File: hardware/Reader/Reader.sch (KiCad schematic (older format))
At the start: 13 parts, among them U1 MAX25276ATCA_VY+, U2 STN2120, X1 16MHz

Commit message: Revised initial schematics for hierarhical structure. Added ESP32, 'Power Supply', Reader MEMs and Power Switch. OBD-II Interpreter is work-in-progress
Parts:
- removed C1, C2: 1uF, symbol Device:C
- removed Cbst1: 0.1uF, symbol Device:C
- removed Cin1: 4.7 uF, symbol Device:CP
- removed Cl1: 0.1 uF, symbol Device:CP
- removed Cout1: 22uF, symbol Device:C
- removed JP1: Reset NVM???, symbol Device:Jumper
- removed L1: 4.7 uH, symbol Device:L
- removed R10, R7: 100k, symbol Device:R
- removed U1: MAX25276ATCA_VY+, 21-100284A_TD1233Y+3C_MXM, symbol MAX25276ATCAVY:MAX25276ATCA_VY+
- removed U2: STN2120, symbol CANtech:STN2120
- removed X1: 16MHz, symbol Device:Crystal_GND24
- added ESP32: NodeMCU_ESP32_DevKit, symbol CANtech:NodeMCU_ESP32_DevKit
- added Rdown: R???, symbol Device:R_Small
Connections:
- net labels added: +5V, GND, Pin10_SAE_J1850_BUS-, Pin11_MS_CAN_Low, Pin12, Pin13, Pin14_ISO15765-4_CAN_BUS_Low, Pin15_ISO9141_L-Line, Pin16_Raw_+12V_Battery, Pin1_SW_CAN, Pin2_SAE_J1850_BUS+, Pin3_MS_CAN_High, Pin4_GnD_Chassis, Pin5_Gnd_Signal, Pin6_ISO15765-4_CAN_BUS_High, Pin7_ISO9141_K-Line, Pin8, Pin9
- net labels removed: +12V, ESP32, GNDPWR, GNDREF
- wire segments 74 -> 38
- no-connect marks 0 -> 4
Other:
- note added: "OBD-II Connector/Data Link Connector"

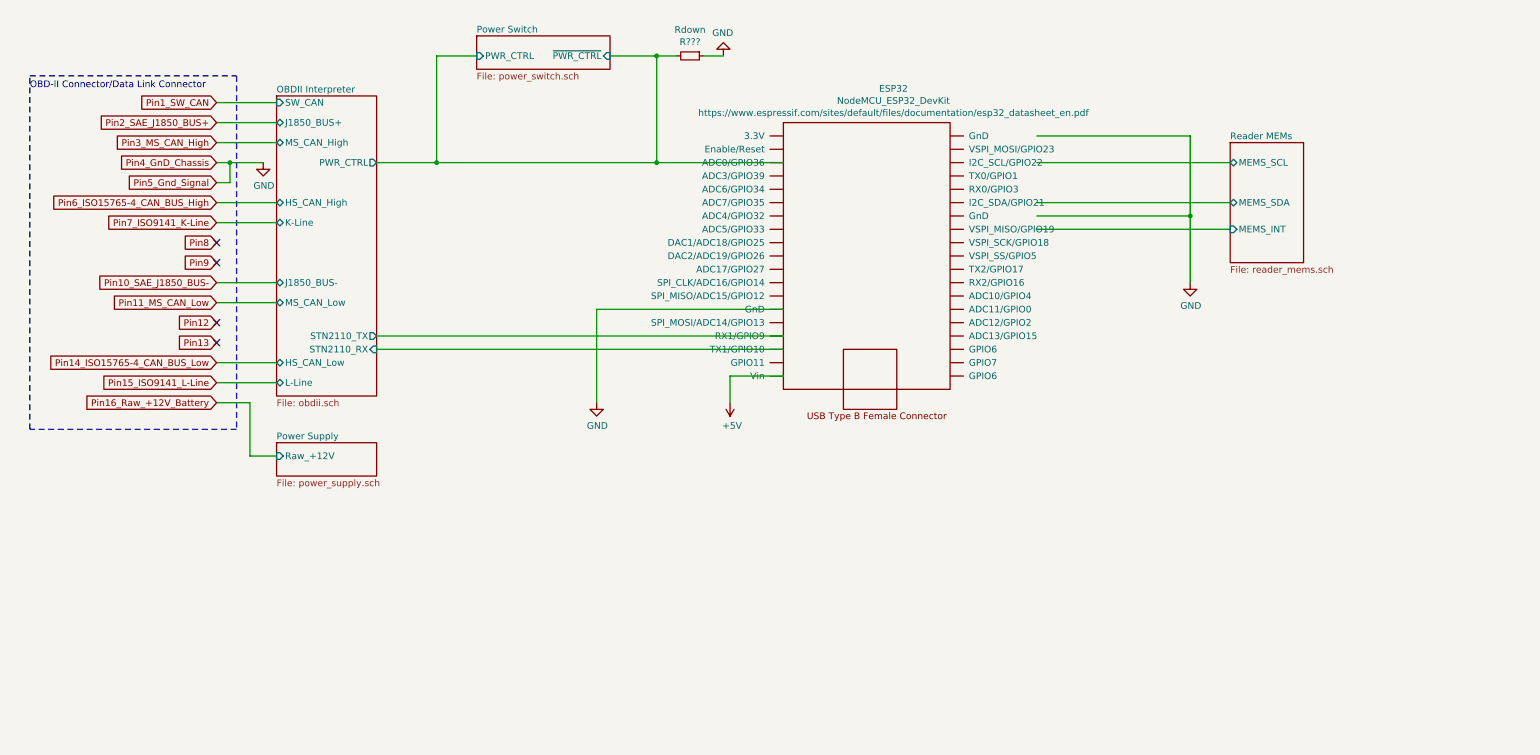
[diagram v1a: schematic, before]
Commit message: Completed schematics for reader
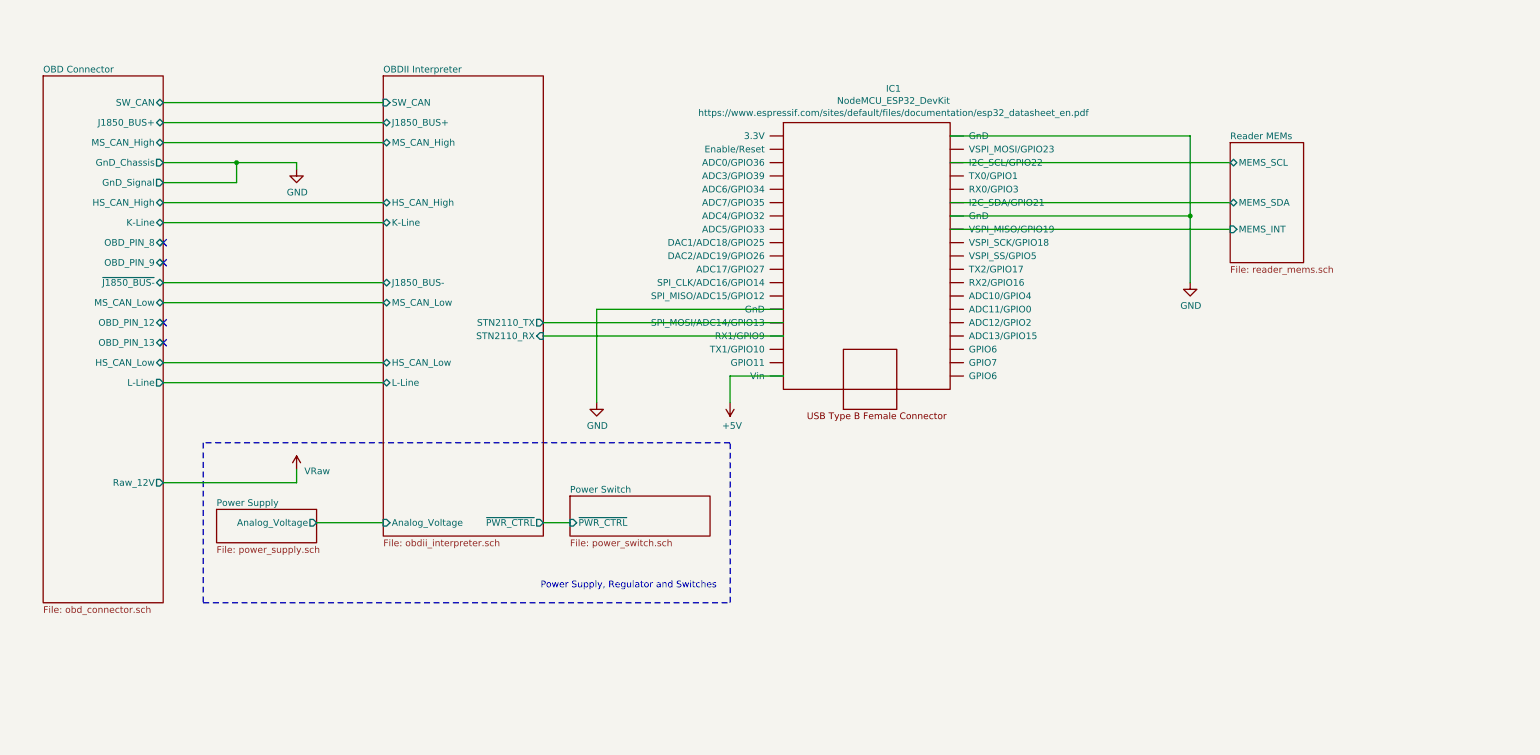
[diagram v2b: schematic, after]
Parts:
- removed Rdown: R???, symbol Device:R_Small
- renumbered ESP32 to IC1
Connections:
- net labels added: VRaw
- net labels removed: Pin10_SAE_J1850_BUS-, Pin11_MS_CAN_Low, Pin12, Pin13, Pin14_ISO15765-4_CAN_BUS_Low, Pin15_ISO9141_L-Line, Pin16_Raw_+12V_Battery, Pin1_SW_CAN, Pin2_SAE_J1850_BUS+, Pin3_MS_CAN_High, Pin4_GnD_Chassis, Pin5_Gnd_Signal, Pin6_ISO15765-4_CAN_BUS_High, Pin7_ISO9141_K-Line, Pin8, Pin9
- wire segments 38 -> 31
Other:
- note added: "Power Supply, Regulator and Switches"
- note removed: "OBD-II Connector/Data Link Connector"
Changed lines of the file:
@@
 $Descr USLetter 11000 8500
 encoding utf-8
-Sheet 1 9
+Sheet 1 17
 Title "CANnect Reader"
-Date "2020-10-18"
+Date "2020-10-20"
 Rev "0.0.1"
 Comp "CANtech"
-Comment1 ""
+Comment1 "Created by Choong Jin Ng | jin8383@gmail.com"
 Comment2 ""
 Comment3 ""
 Comment4 ""
 $EndDescr
-Text GLabel 2000 3650 0    50   Input ~ 0
-Pin16_Raw_+12V_Battery
-Text GLabel 2000 1850 0    50   Input ~ 0
-Pin4_GnD_Chassis
-Text GLabel 2000 2000 0    50   Input ~ 0
-Pin5_Gnd_Signal
-Text GLabel 2000 2450 0    50   Input ~ 0
-Pin8
-Text GLabel 2000 2600 0    50   Input ~ 0
-Pin9
-Text GLabel 2000 3050 0    50   Input ~ 0
-Pin12
-Text GLabel 2000 3200 0    50   Input ~ 0
-Pin13
-NoConn ~ 2000 3050
-NoConn ~ 2000 3200
-NoConn ~ 2000 2600
-NoConn ~ 2000 2450
-Wire Wire Line
-	2000 1850 2100 1850
-Wire Wire Line
-	2000 2000 2100 2000
-Wire Wire Line
-	2100 2000 2100 1850
-Connection ~ 2100 1850
-Wire Wire Line
-	2100 1850 2350 1850
-$Comp
-L power:GND #PWR0101
-U 1 1 5F8F20F1
-P 2350 1850
-F 0 "#PWR0101" H 2350 1600 50  0001 C CNN
-F 1 "GND" H 2355 1677 50  0000 C CNN
-F 2 "" H 2350 1850 50  0001 C CNN
-F 3 "" H 2350 1850 50  0001 C CNN
-	1    2350 1850
-	1    0    0    -1
-$EndComp
 $Comp
 L power:GND #PWR0102
@@
 $EndComp
 $Sheet
-S 2450 3950 750  250
+S 2000 4450 750  250
 U 5F8ADA45
 F0 "Power Supply" 50
 F1 "power_supply.sch" 50
-F2 "Raw_+12V" I L 2450 4050 50
+F2 "Analog_Voltage" O R 2750 4550 50
 $EndSheet
 Wire Wire Line
@@
 Wire Wire Line
 	9300 2250 9300 2750
-Text GLabel 2000 2900 0    50   Input ~ 0
-Pin11_MS_CAN_Low
-Text GLabel 2000 1700 0    50   Input ~ 0
-Pin3_MS_CAN_High
-Text GLabel 2000 2750 0    50   Input ~ 0
-Pin10_SAE_J1850_BUS-
-Text GLabel 2000 1550 0    50   Input ~ 0
-Pin2_SAE_J1850_BUS+
-Text GLabel 2000 3350 0    50   Input ~ 0
-Pin14_ISO15765-4_CAN_BUS_Low
-Text GLabel 2000 2150 0    50   Input ~ 0
-Pin6_ISO15765-4_CAN_BUS_High
-Text GLabel 2000 3500 0    50   Input ~ 0
-Pin15_ISO9141_L-Line
-Text GLabel 2000 2300 0    50   Input ~ 0
-Pin7_ISO9141_K-Line
-Wire Wire Line
-	2000 2900 2450 2900
-Wire Wire Line
-	2000 1700 2450 1700
-Wire Wire Line
-	2000 2750 2450 2750
-Wire Wire Line
-	2000 1550 2450 1550
-Wire Wire Line
-	2000 3350 2450 3350
-Wire Wire Line
-	2000 2150 2450 2150
-Wire Wire Line
-	2000 3500 2450 3500
-Wire Wire Line
-	2000 2300 2450 2300
-Text GLabel 2000 1400 0    50   Input ~ 0
-Pin1_SW_CAN
-Wire Wire Line
-	2000 1400 2450 1400
-$Sheet
-S 2450 1350 750  2250
-U 5F95F80B
-F0 "OBDII Interpreter" 50
-F1 "obdii.sch" 50
-F2 "K-Line" B L 2450 2300 50
-F3 "L-Line" B L 2450 3500 50
-F4 "SW_CAN" I L 2450 1400 50
-F5 "J1850_BUS+" B L 2450 1550 50
-F6 "J1850_BUS-" B L 2450 2750 50
-F7 "MS_CAN_High" B L 2450 1700 50
-F8 "MS_CAN_Low" B L 2450 2900 50
-F9 "STN2110_TX" O R 3200 3150 50
-F10 "PWR_CTRL" O R 3200 1850 50
-F11 "HS_CAN_High" B L 2450 2150 50
-F12 "HS_CAN_Low" B L 2450 3350 50
-F13 "STN2110_RX" I R 3200 3250 50
-$EndSheet
-$Sheet
-S 3950 900  1000 250
+$Sheet
+S 4650 4350 1050 300
 U 5FA56A4E
 F0 "Power Switch" 50
 F1 "power_switch.sch" 50
-F2 "~PWR_CTRL~" I R 4950 1050 50
-F3 "PWR_CTRL" I L 3950 1050 50
+F2 "~PWR_CTRL~" I L 4650 4550 50
 $EndSheet
 $Sheet
@@
 F4 "MEMS_INT" I L 9600 2350 50
 $EndSheet
-Wire Wire Line
-	8150 2350 9600 2350
-Wire Wire Line
-	8150 2150 9600 2150
-Wire Wire Line
-	8150 1650 9300 1650
-Wire Wire Line
-	8150 2250 9300 2250
-Wire Wire Line
-	8150 1850 9600 1850
 $Comp
 L power:GND #PWR0104
@@
 	1    0    0    1
 $EndComp
-$Comp
-L CANtech:NodeMCU_ESP32_DevKit ESP32
+Wire Wire Line
+	5850 3650 5850 3450
+Wire Wire Line
+	5850 3450 6250 3450
+Wire Wire Line
+	4850 3650 4850 2950
+Wire Wire Line
+	4850 2950 6250 2950
+$Comp
+L CANtech:VRaw #V0101
+U 1 1 5FD58425
+P 2600 4100
+F 0 "#V0101" H 2600 4100 50  0001 C CNN
+F 1 "VRaw" H 2658 4037 50  0000 L CNN
+F 2 "" H 2600 4100 50  0001 C CNN
+F 3 "" H 2600 4100 50  0001 C CNN
+	1    2600 4100
+	1    0    0    -1
+$EndComp
+$Comp
+L CANtech:NodeMCU_ESP32_DevKit IC1
 U 1 1 5F91A3F3
 P 6900 4900
-F 0 "ESP32" H 7075 8505 50  0000 C CNN
+F 0 "IC1" H 7075 8505 50  0000 C CNN
 F 1 "NodeMCU_ESP32_DevKit" H 7075 8414 50  0000 C CNN
 F 2 "" H 6900 4900 50  0001 C CNN
@@
 $EndComp
 Wire Wire Line
-	5850 3650 5850 3450
-Wire Wire Line
-	5850 3450 6250 3450
-Wire Wire Line
-	4850 3650 4850 2950
-Wire Wire Line
-	4850 2950 6250 2950
-$Comp
-L power:GND #PWR?
-U 1 1 5FA7F77A
-P 5800 1050
-F 0 "#PWR?" H 5800 800 50  0001 C CNN
-F 1 "GND" H 5805 877 50  0000 C CNN
-F 2 "" H 5800 1050 50  0001 C CNN
-F 3 "" H 5800 1050 50  0001 C CNN
-	1    5800 1050
-	-1   0    0    1
-$EndComp
-Wire Wire Line
-	6250 1850 5300 1850
-Wire Wire Line
-	5300 1850 5300 1050
-Wire Wire Line
-	4950 1050 5300 1050
-$Comp
-L Device:R_Small Rdown
-U 1 1 5FA811AB
-P 5550 1050
-F 0 "Rdown" V 5354 1050 50  0000 C CNN
-F 1 "R???" V 5445 1050 50  0000 C CNN
-F 2 "" H 5550 1050 50  0001 C CNN
-F 3 "~" H 5550 1050 50  0001 C CNN
-	1    5550 1050
-	0    1    1    0
-$EndComp
-Wire Wire Line
-	5300 1050 5450 1050
-Connection ~ 5300 1050
-Wire Wire Line
-	5650 1050 5800 1050
-Wire Wire Line
-	5300 1850 3650 1850
-Connection ~ 5300 1850
-Wire Wire Line
-	3950 1050 3650 1050
-Wire Wire Line
-	3650 1050 3650 1850
-Connection ~ 3650 1850
-Wire Wire Line
-	3650 1850 3200 1850
-Wire Wire Line
-	3200 3150 6250 3150
-Wire Wire Line
-	6250 3250 3200 3250
-Wire Wire Line
-	2000 3650 2250 3650
-Wire Wire Line
-	2250 3650 2250 4050
-Wire Wire Line
-	2250 4050 2450 4050
-Wire Notes Line
-	2150 1200 2150 3850
-Wire Notes Line
-	2150 3850 600  3850
-Wire Notes Line
-	600  3850 600  1200
-Wire Notes Line
-	600  1200 2150 1200
-Text Notes 600  1300 0    50   ~ 0
-OBD-II Connector/Data Link Connector
+	2600 4250 2600 4150
+Wire Wire Line
+	2750 4550 3250 4550
+$Sheet
+S 3250 1200 1200 3450
+U 5F95F80B
+F0 "OBDII Interpreter" 50
+F1 "obdii_interpreter.sch" 50
+F2 "K-Line" B L 3250 2300 50
+F3 "L-Line" B L 3250 3500 50
+F4 "SW_CAN" I L 3250 1400 50
+F5 "J1850_BUS+" B L 3250 1550 50
+F6 "J1850_BUS-" B L 3250 2750 50
+F7 "MS_CAN_High" B L 3250 1700 50
+F8 "MS_CAN_Low" B L 3250 2900 50
+F9 "STN2110_TX" O R 4450 3050 50
+F10 "HS_CAN_High" B L 3250 2150 50
+F11 "HS_CAN_Low" B L 3250 3350 50
+F12 "STN2110_RX" I R 4450 3150 50
+F13 "~PWR_CTRL~" O R 4450 4550 50
+F14 "Analog_Voltage" I L 3250 4550 50
+$EndSheet
+Wire Wire Line
+	4450 4550 4650 4550
+Wire Notes Line
+	1900 3950 1900 5150
+Wire Notes Line
+	1900 5150 5850 5150
+Wire Notes Line
+	5850 5150 5850 3950
+Wire Notes Line
+	5850 3950 1900 3950
+Text Notes 5750 5050 2    50   ~ 0
+Power Supply, Regulator and Switches
+Wire Wire Line
+	4450 3050 6250 3050
+Wire Wire Line
+	6250 3150 4450 3150
+$Sheet
+S 700  1200 900  3950
+U 5FF6FE24
+F0 "OBD Connector" 50
+F1 "obd_connector.sch" 50
+F2 "SW_CAN" B R 1600 1400 50
+F3 "Raw_12V" O R 1600 4250 50
+F4 "J1850_BUS+" B R 1600 1550 50
+F5 "MS_CAN_High" B R 1600 1700 50
+F6 "GnD_Chassis" O R 1600 1850 50
+F7 "GnD_Signal" O R 1600 2000 50
+F8 "HS_CAN_High" B R 1600 2150 50
+F9 "K-Line" B R 1600 2300 50
+F10 "OBD_PIN_8" B R 1600 2450 50
+F11 "OBD_PIN_9" B R 1600 2600 50
+F12 "~J1850_BUS-~" B R 1600 2750 50
+F13 "MS_CAN_Low" B R 1600 2900 50
+F14 "OBD_PIN_12" B R 1600 3050 50
+F15 "OBD_PIN_13" B R 1600 3200 50
+F16 "HS_CAN_Low" B R 1600 3350 50
+F17 "L-Line" O R 1600 3500 50
+$EndSheet
+Wire Wire Line
+	1600 4250 2600 4250
+Wire Wire Line
+	1600 1400 3250 1400
+Wire Wire Line
+	1600 1550 3250 1550
+Wire Wire Line
+	3250 1700 1600 1700
+$Comp
+L power:GND #PWR01
+U 1 1 5FF8C892
+P 2600 1900
+F 0 "#PWR01" H 2600 1650 50  0001 C CNN
+F 1 "GND" H 2605 1727 50  0000 C CNN
+F 2 "" H 2600 1900 50  0001 C CNN
+F 3 "" H 2600 1900 50  0001 C CNN
+	1    2600 1900
+	1    0    0    -1
+$EndComp
+Wire Wire Line
+	1600 1850 2150 1850
+Wire Wire Line
+	2600 1850 2600 1900
+Wire Wire Line
+	1600 2000 2150 2000
+Wire Wire Line
+	2150 2000 2150 1850
+Connection ~ 2150 1850
+Wire Wire Line
+	2150 1850 2600 1850
+Wire Wire Line
+	1600 2150 3250 2150
+Wire Wire Line
+	1600 2300 3250 2300
+Wire Wire Line
+	1600 2750 3250 2750
+Wire Wire Line
+	3250 2900 1600 2900
+Wire Wire Line
+	1600 3350 3250 3350
+Wire Wire Line
+	3250 3500 1600 3500
+NoConn ~ 1600 2450
+NoConn ~ 1600 2600
+NoConn ~ 1600 3050
+NoConn ~ 1600 3200
+Wire Wire Line
+	7500 1650 9300 1650
+Wire Wire Line
+	7500 2150 9600 2150
+Wire Wire Line
+	7500 2250 9300 2250
+Wire Wire Line
+	7500 2350 9600 2350
+Wire Wire Line
+	7500 1850 9600 1850
 $EndSCHEMATC

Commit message: Completed Reader schematics for version 0.0.01
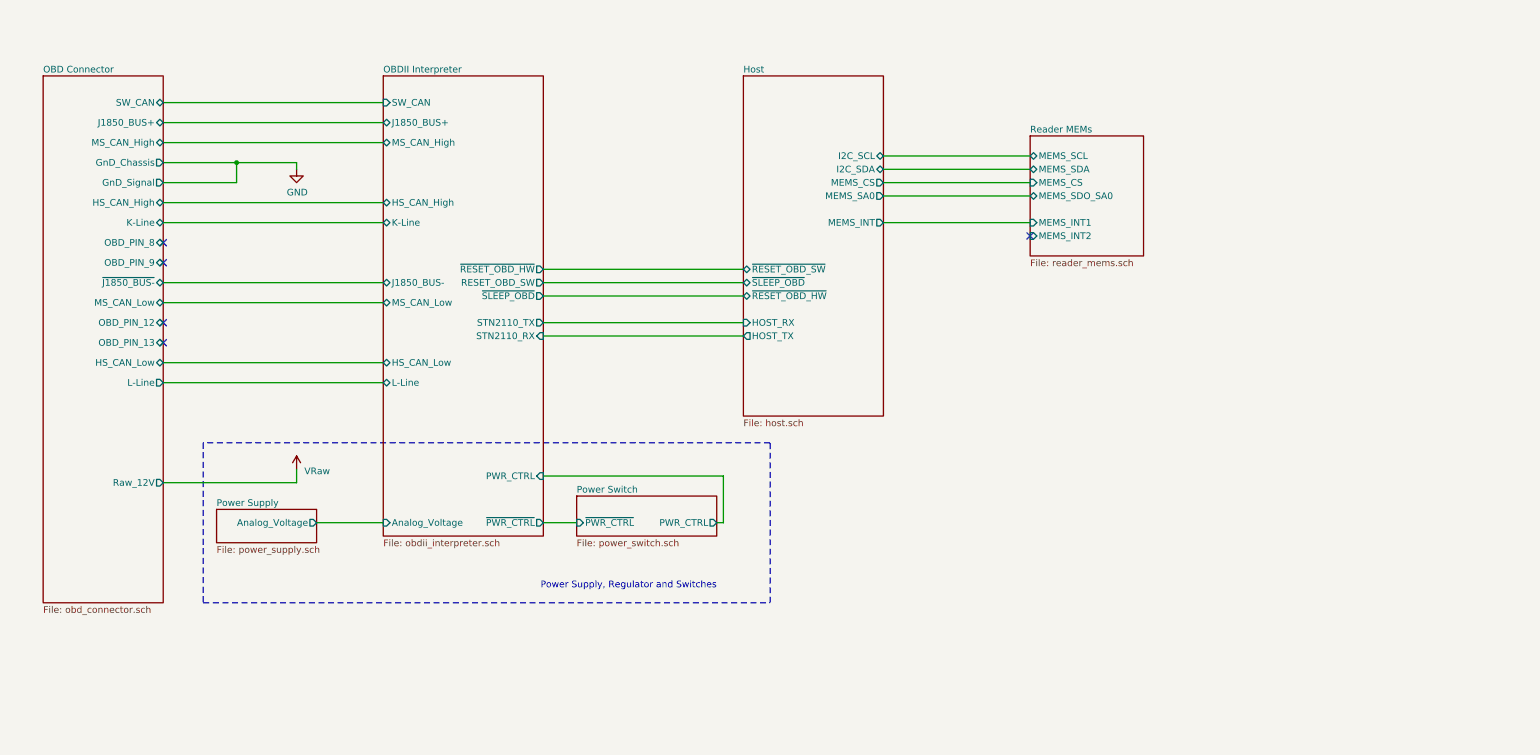
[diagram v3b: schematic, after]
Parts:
- removed IC1: NodeMCU_ESP32_DevKit, symbol CANtech:NodeMCU_ESP32_DevKit
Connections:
- no-connect marks 4 -> 5
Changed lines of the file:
@@
 $Descr USLetter 11000 8500
 encoding utf-8
-Sheet 1 17
+Sheet 1 18
 Title "CANnect Reader"
 Date "2020-10-20"
-Rev "0.0.1"
+Rev "0.0.01"
 Comp "CANtech"
 Comment1 "Created by Choong Jin Ng | jin8383@gmail.com"
@@
 Comment4 ""
 $EndDescr
-$Comp
-L power:GND #PWR0102
-U 1 1 5F9AA491
-P 9300 2750
-F 0 "#PWR0102" H 9300 2500 50  0001 C CNN
-F 1 "GND" H 9305 2577 50  0000 C CNN
-F 2 "" H 9300 2750 50  0001 C CNN
-F 3 "" H 9300 2750 50  0001 C CNN
-	1    9300 2750
-	1    0    0    -1
-$EndComp
 $Sheet
 S 2000 4450 750  250
@@
 F2 "Analog_Voltage" O R 2750 4550 50
 $EndSheet
-Wire Wire Line
-	9300 1650 9300 2250
-Connection ~ 9300 2250
-Wire Wire Line
-	9300 2250 9300 2750
-$Sheet
-S 4650 4350 1050 300
+$Sheet
+S 4700 4350 1050 300
 U 5FA56A4E
 F0 "Power Switch" 50
 F1 "power_switch.sch" 50
-F2 "~PWR_CTRL~" I L 4650 4550 50
-$EndSheet
-$Sheet
-S 9600 1700 550  900
-U 5F988046
-F0 "Reader MEMs" 50
-F1 "reader_mems.sch" 50
-F2 "MEMS_SCL" B L 9600 1850 50
-F3 "MEMS_SDA" B L 9600 2150 50
-F4 "MEMS_INT" I L 9600 2350 50
-$EndSheet
-$Comp
-L power:GND #PWR0104
-U 1 1 5FA13F0A
-P 4850 3650
-F 0 "#PWR0104" H 4850 3400 50  0001 C CNN
-F 1 "GND" H 4855 3477 50  0000 C CNN
-F 2 "" H 4850 3650 50  0001 C CNN
-F 3 "" H 4850 3650 50  0001 C CNN
-	1    4850 3650
-	1    0    0    -1
-$EndComp
-$Comp
-L power:+5V #PWR0103
-U 1 1 5FA10F8A
-P 5850 3650
-F 0 "#PWR0103" H 5850 3500 50  0001 C CNN
-F 1 "+5V" H 5865 3823 50  0000 C CNN
-F 2 "" H 5850 3650 50  0001 C CNN
-F 3 "" H 5850 3650 50  0001 C CNN
-	1    5850 3650
-	1    0    0    1
-$EndComp
-Wire Wire Line
-	5850 3650 5850 3450
-Wire Wire Line
-	5850 3450 6250 3450
-Wire Wire Line
-	4850 3650 4850 2950
-Wire Wire Line
-	4850 2950 6250 2950
+F2 "~PWR_CTRL~" I L 4700 4550 50
+F3 "PWR_CTRL" O R 5750 4550 50
+$EndSheet
 $Comp
 L CANtech:VRaw #V0101
@@
 F 3 "" H 2600 4100 50  0001 C CNN
 	1    2600 4100
-	1    0    0    -1
-$EndComp
-$Comp
-L CANtech:NodeMCU_ESP32_DevKit IC1
-U 1 1 5F91A3F3
-P 6900 4900
-F 0 "IC1" H 7075 8505 50  0000 C CNN
-F 1 "NodeMCU_ESP32_DevKit" H 7075 8414 50  0000 C CNN
-F 2 "" H 6900 4900 50  0001 C CNN
-F 3 "" H 6900 4900 50  0001 C CNN
-F 4 "https://www.espressif.com/sites/default/files/documentation/esp32_datasheet_en.pdf" H 7075 8323 50  0000 C CNN "Website"
-	1    6900 4900
 	1    0    0    -1
 $EndComp
@@
 F13 "~PWR_CTRL~" O R 4450 4550 50
 F14 "Analog_Voltage" I L 3250 4550 50
-$EndSheet
-Wire Wire Line
-	4450 4550 4650 4550
+F15 "~SLEEP_OBD~" O R 4450 2850 50
+F16 "RESET_OBD_SW" O R 4450 2750 50
+F17 "~RESET_OBD_HW~" O R 4450 2650 50
+F18 "PWR_CTRL" I R 4450 4200 50
+$EndSheet
 Wire Notes Line
 	1900 3950 1900 5150
 Wire Notes Line
-	1900 5150 5850 5150
-Wire Notes Line
-	5850 5150 5850 3950
-Wire Notes Line
-	5850 3950 1900 3950
+	1900 5150 6150 5150
+Wire Notes Line
+	6150 5150 6150 3950
+Wire Notes Line
+	6150 3950 1900 3950
 Text Notes 5750 5050 2    50   ~ 0
 Power Supply, Regulator and Switches
-Wire Wire Line
-	4450 3050 6250 3050
-Wire Wire Line
-	6250 3150 4450 3150
 $Sheet
 S 700  1200 900  3950
@@
 	3250 2900 1600 2900
 Wire Wire Line
-	1600 3350 3250 3350
-Wire Wire Line
 	3250 3500 1600 3500
 NoConn ~ 1600 2450
@@
 NoConn ~ 1600 3200
 Wire Wire Line
-	7500 1650 9300 1650
-Wire Wire Line
-	7500 2150 9600 2150
-Wire Wire Line
-	7500 2250 9300 2250
-Wire Wire Line
-	7500 2350 9600 2350
-Wire Wire Line
-	7500 1850 9600 1850
+	4450 4550 4700 4550
+Wire Wire Line
+	5750 4550 5800 4550
+Wire Wire Line
+	5800 4550 5800 4200
+Wire Wire Line
+	5800 4200 4450 4200
+Wire Wire Line
+	1600 3350 3250 3350
+Wire Wire Line
+	5950 2650 4450 2650
+Wire Wire Line
+	4450 2750 5950 2750
+Wire Wire Line
+	5950 2850 4450 2850
+Wire Wire Line
+	8100 2300 7000 2300
+Wire Wire Line
+	7000 2100 8100 2100
+Wire Wire Line
+	7000 1800 8100 1800
+Wire Wire Line
+	5950 3150 4450 3150
+Wire Wire Line
+	4450 3050 5950 3050
+$Sheet
+S 5950 1200 1050 2550
+U 5F91C7D3
+F0 "Host" 50
+F1 "host.sch" 50
+F2 "HOST_RX" I L 5950 3050 50
+F3 "HOST_TX" O L 5950 3150 50
+F4 "I2C_SCL" B R 7000 1800 50
+F5 "I2C_SDA" B R 7000 1900 50
+F6 "MEMS_INT" O R 7000 2300 50
+F7 "~SLEEP_OBD~" B L 5950 2750 50
+F8 "~RESET_OBD_SW~" B L 5950 2650 50
+F9 "~RESET_OBD_HW~" B L 5950 2850 50
+F10 "MEMS_CS" O R 7000 2000 50
+F11 "MEMS_SA0" O R 7000 2100 50
+$EndSheet
+NoConn ~ 8100 2400
+Wire Wire Line
+	7000 1900 8100 1900
+Wire Wire Line
+	7000 2000 8100 2000
+$Sheet
+S 8100 1650 850  900
+U 5F988046
+F0 "Reader MEMs" 50
+F1 "reader_mems.sch" 50
+F2 "MEMS_SCL" B L 8100 1800 50
+F3 "MEMS_SDA" B L 8100 1900 50
+F4 "MEMS_INT1" I L 8100 2300 50
+F5 "MEMS_CS" I L 8100 2000 50
+F6 "MEMS_SDO_SA0" B L 8100 2100 50
+F7 "MEMS_INT2" I L 8100 2400 50
+$EndSheet
 $EndSCHEMATC
